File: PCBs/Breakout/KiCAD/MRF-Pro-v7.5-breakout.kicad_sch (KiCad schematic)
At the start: 3 parts, among them J5 FPC 8P Connector, J6 Stemma QT, J7 TFS20L / DTS6012M

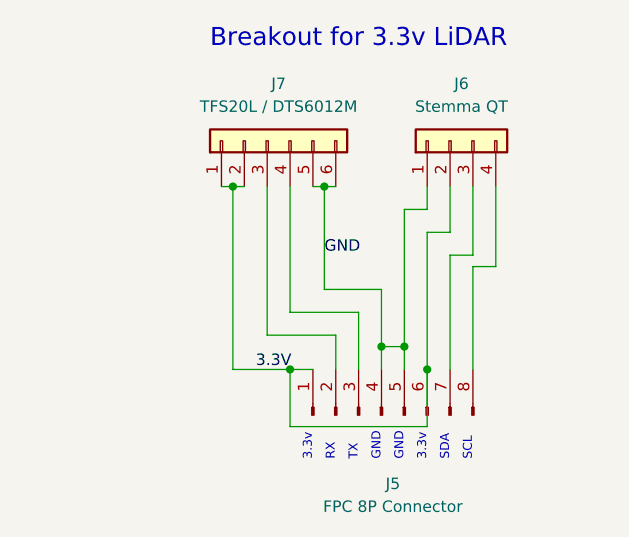
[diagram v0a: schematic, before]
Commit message: Add LiDAR decoupling to breakout schematic
Stage 1 of the breakout respin for the LiDAR power-droop issue. Adds a
decoupling network across the LiDAR 3.3V rail at J7: C1 47uF bulk, C2 1uF,
C3 100nF. ERC is clean and the netlist confirms all three sit on the 3.3V
and GND nets alongside the LiDAR connector.

The schematic is intentionally ahead of the PCB; the board layout
(placement at J7, wider copper, ground stitching, DRC, fab outputs) is
captured as a step-by-step in the new breakout layout spec for completion
in the KiCad PCB editor.

Tracing the current board also showed J7 already separates the sensor's two
supply pins and the FPC has no spare conductors, which is recorded in the
errata for the gated dedicated-regulator stage.
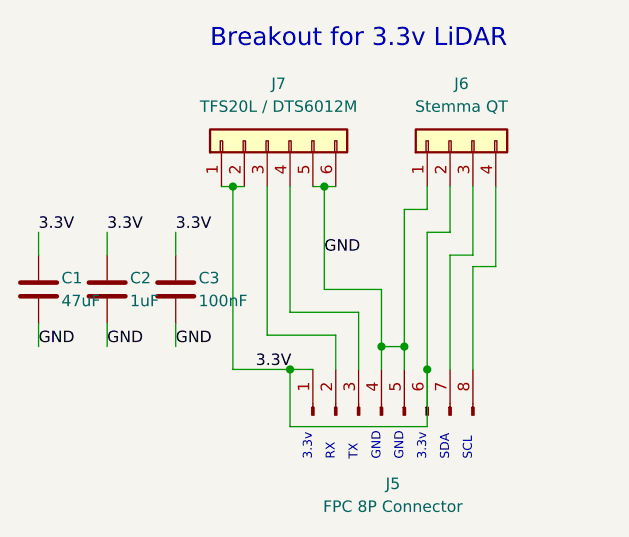
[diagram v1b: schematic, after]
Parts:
- added C1: 47uF, Capacitor_SMD:C_1206_3216Metric, symbol Device:C
- added C2: 1uF, Capacitor_SMD:C_0603_1608Metric, symbol Device:C
- added C3: 100nF, Capacitor_SMD:C_0402_1005Metric, symbol Device:C
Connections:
- net 3.3V: now also C1.1, C2.1, C3.1
- net GND: now also C1.2, C2.2, C3.2
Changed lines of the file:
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@@
 		)
 	)
+	(symbol
+		(lib_id "Device:C")
+		(at 114.3 93.98 0)
+		(unit 1)
+		(exclude_from_sim no)
+		(in_bom yes)
+		(on_board yes)
+		(dnp no)
+		(property "Reference" "C1"
+			(at 116.84 92.71000000000001 0)
+			(effects (font (size 1.27 1.27)) (justify left))
+		)
+		(property "Value" "47uF"
+			(at 116.84 95.25 0)
+			(effects (font (size 1.27 1.27)) (justify left))
+		)
+		(property "Footprint" "Capacitor_SMD:C_1206_3216Metric"
+			(at 114.3 93.98 0)
+			(effects (font (size 1.27 1.27)) (hide yes))
+		)
+		(property "Datasheet" "~"
+			(at 114.3 93.98 0)
+			(effects (font (size 1.27 1.27)) (hide yes))
+		)
+		(property "Description" "Unpolarized capacitor"
+			(at 114.3 93.98 0)
+			(effects (font (size 1.27 1.27)) (hide yes))
+		)
+		(pin "1")
+		(pin "2")
+		(instances
+			(project "MRF-Pro-v7-breakout-33"
+				(path "/896eaae8-6acf-41d9-a1f7-3a80349c3bd9"
+					(reference "C1")
+					(unit 1)
+				)
+			)
+		)
+	)
+	(wire (pts (xy 114.3 90.17) (xy 114.3 87.63)) (stroke (width 0) (type default)))
+	(wire (pts (xy 114.3 97.79) (xy 114.3 100.33000000000001)) (stroke (width 0) (type default)))
+	(label "3.3V" (at 114.3 87.63 0) (effects (font (size 1.27 1.27)) (justify left bottom)))
+	(label "GND" (at 114.3 100.33000000000001 0) (effects (font (size 1.27 1.27)) (justify left bottom)))
+	(symbol
+		(lib_id "Device:C")
+		(at 121.92 93.98 0)
+		(unit 1)
+		(exclude_from_sim no)
+		(in_bom yes)
+		(on_board yes)
+		(dnp no)
+		(property "Reference" "C2"
+			(at 124.46000000000001 92.71000000000001 0)
+			(effects (font (size 1.27 1.27)) (justify left))
+		)
+		(property "Value" "1uF"
+			(at 124.46000000000001 95.25 0)
+			(effects (font (size 1.27 1.27)) (justify left))
+		)
+		(property "Footprint" "Capacitor_SMD:C_0603_1608Metric"
+			(at 121.92 93.98 0)
+			(effects (font (size 1.27 1.27)) (hide yes))
+		)
+		(property "Datasheet" "~"
+			(at 121.92 93.98 0)
+			(effects (font (size 1.27 1.27)) (hide yes))
+		)
+		(property "Description" "Unpolarized capacitor"
+			(at 121.92 93.98 0)
+			(effects (font (size 1.27 1.27)) (hide yes))
+		)
+		(pin "1")
+		(pin "2")
+		(instances
+			(project "MRF-Pro-v7-breakout-33"
+				(path "/896eaae8-6acf-41d9-a1f7-3a80349c3bd9"
+					(reference "C2")
+					(unit 1)
+				)
+			)
+		)
+	)
+	(wire (pts (xy 121.92 90.17) (xy 121.92 87.63)) (stroke (width 0) (type default)))
+	(wire (pts (xy 121.92 97.79) (xy 121.92 100.33000000000001)) (stroke (width 0) (type default)))
+	(label "3.3V" (at 121.92 87.63 0) (effects (font (size 1.27 1.27)) (justify left bottom)))
+	(label "GND" (at 121.92 100.33000000000001 0) (effects (font (size 1.27 1.27)) (justify left bottom)))
+	(symbol
+		(lib_id "Device:C")
+		(at 129.54 93.98 0)
+		(unit 1)
+		(exclude_from_sim no)
+		(in_bom yes)
+		(on_board yes)
+		(dnp no)
+		(property "Reference" "C3"
+			(at 132.07999999999998 92.71000000000001 0)
+			(effects (font (size 1.27 1.27)) (justify left))
+		)
+		(property "Value" "100nF"
+			(at 132.07999999999998 95.25 0)
+			(effects (font (size 1.27 1.27)) (justify left))
+		)
+		(property "Footprint" "Capacitor_SMD:C_0402_1005Metric"
+			(at 129.54 93.98 0)
+			(effects (font (size 1.27 1.27)) (hide yes))
+		)
+		(property "Datasheet" "~"
+			(at 129.54 93.98 0)
+			(effects (font (size 1.27 1.27)) (hide yes))
+		)
+		(property "Description" "Unpolarized capacitor"
+			(at 129.54 93.98 0)
+			(effects (font (size 1.27 1.27)) (hide yes))
+		)
+		(pin "1")
+		(pin "2")
+		(instances
+			(project "MRF-Pro-v7-breakout-33"
+				(path "/896eaae8-6acf-41d9-a1f7-3a80349c3bd9"
+					(reference "C3")
+					(unit 1)
+				)
+			)
+		)
+	)
+	(wire (pts (xy 129.54 90.17) (xy 129.54 87.63)) (stroke (width 0) (type default)))
+	(wire (pts (xy 129.54 97.79) (xy 129.54 100.33000000000001)) (stroke (width 0) (type default)))
+	(label "3.3V" (at 129.54 87.63 0) (effects (font (size 1.27 1.27)) (justify left bottom)))
+	(label "GND" (at 129.54 100.33000000000001 0) (effects (font (size 1.27 1.27)) (justify left bottom)))
 	(sheet_instances
 		(path "/"
